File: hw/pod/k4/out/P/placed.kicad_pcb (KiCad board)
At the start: 6 copper layers, 15.5 x 12 mm, 37 parts, among them J1 TestPoint_Pad_D1.0mm, J2 TestPoint_Pad_D1.0mm, J21 CONN-SMD_BM28B0.6-30DP-2-0.35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, Q1 Nexperia_SOT1216_DFN1010B-6, Q2 Nexperia_SOT1216_DFN1010B-6, U1 QFN-48-1EP_7x7mm_P0.5mm_EP5.6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, Y1 Crystal_SMD_2012-2Pin_2.0x1.2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

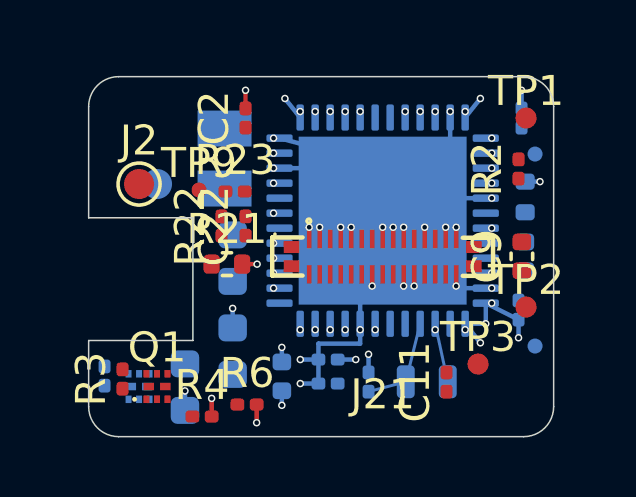
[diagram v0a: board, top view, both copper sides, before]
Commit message: K4 lid ledge 0.70 (ECR-0022) + C21 0402: M re-routed 0/0, heights from datasheets: lid +0.112 floor +0.163 worst, B2B gap side still fails (C16 -0.10, C17/C9 -0.05)
Noise F02->MIC_VDD worst corner 28.7 dB, k4_checks PASS, plm 0/0. P untouched.

Co-Authored-By: Claude Opus 5.5 <noreply@anthropic.com>
Claude-Session: https://claude.ai/code/session_01Wg997D6KFs8bxoAH56jZZJ
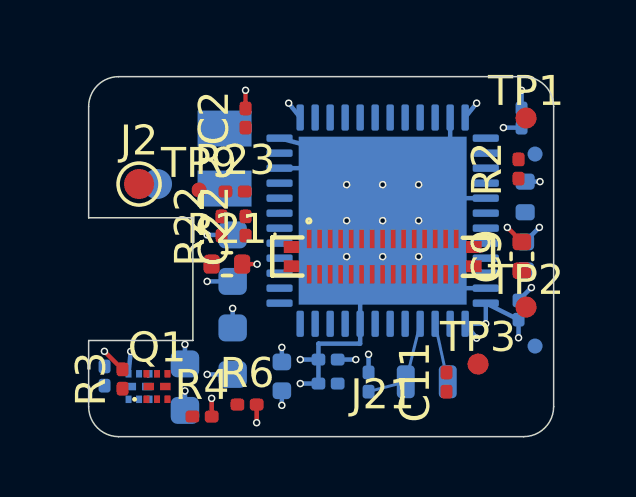
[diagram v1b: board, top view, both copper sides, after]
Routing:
- net GND: track 15.4 -> 18.9 mm, vias 31 -> 25
- net +3V0: track 7.38 -> 10.7 mm, vias 14 -> 13
- net VDD11: vias 2 -> 0
- net VBUS_SENSE: vias 1 -> 0
- net VBAT_SENSE: vias 1 -> 0
- net USB_DP: vias 1 -> 0
- net USB_DM: vias 1 -> 0
- net TS: vias 1 -> 0
- net SWDIO: vias 1 -> 0
- net SWCLK: vias 1 -> 0
- net NRST: vias 1 -> 0
- net N$2: vias 1 -> 0
- net MIC_VDD: vias 1 -> 0
- net MIC_DATA: vias 1 -> 0
- net MDF_SDI: vias 1 -> 0
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
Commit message: K4 guide: BM28 no-key warning, pin-1 dots, photo check, 10-cycle limit
Co-Authored-By: Claude Opus 5.5 <noreply@anthropic.com>
Claude-Session: https://claude.ai/code/session_01Wg997D6KFs8bxoAH56jZZJ
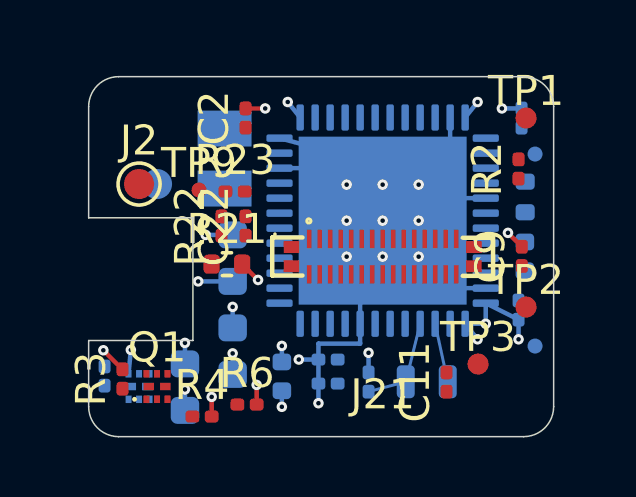
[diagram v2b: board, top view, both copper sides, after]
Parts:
- C9: value C_0402_1005Metric -> C_0201_0603Metric; footprint C_0402_1005Metric -> C_0201_0603Metric
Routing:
- net +3V0: track 10.7 -> 9.78 mm, vias 13 -> 11
- net GND: track 18.9 -> 18.1 mm, vias 25 -> 22
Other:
- copper layers 6 -> 4

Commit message: K4 B2B gap: C16/C17 (M) and C9 (P) to Samsung 0201 (0.39 max): gap side 0 fail, worst +0.05 (U3 BQ25180 / D4 0.5 max are package-fixed); D5 0.45, U3 0.5 from datasheets; M re-routed 0/0, P local edit
Co-Authored-By: Claude Opus 5.5 <noreply@anthropic.com>
Claude-Session: https://claude.ai/code/session_01Wg997D6KFs8bxoAH56jZZJ
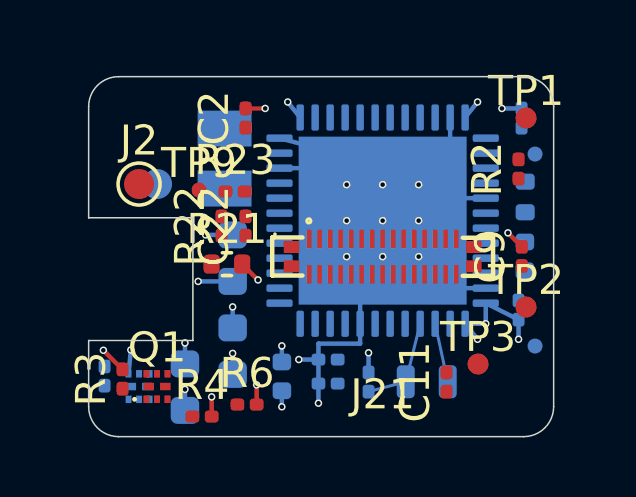
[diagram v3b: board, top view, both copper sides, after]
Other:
- copper layers 4 -> 6
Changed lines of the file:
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@@
 		(4 "In1.Cu" power)
 		(6 "In2.Cu" power)
+		(8 "In3.Cu" signal)
+		(10 "In4.Cu" signal)
 		(2 "B.Cu" signal)
 		(9 "F.Adhes" user "F.Adhesive")
@@
 	(via
 		(at 4.8 9.225)
-		(size 0.35)
+		(size 0.25)
 		(drill 0.15)
 		(layers "F.Cu" "B.Cu")
@@
 	(via
 		(at 6.439999 11.004999)
-		(size 0.35)
+		(size 0.25)
 		(drill 0.15)
 		(layers "F.Cu" "B.Cu")
@@
 	(via
 		(at 6.636139 0.845174)
-		(size 0.35)
+		(size 0.25)
 		(drill 0.15)
 		(layers "F.Cu" "B.Cu")
@@
 	(via
 		(at 14.33 8.754999)
-		(size 0.35)
+		(size 0.25)
 		(drill 0.15)
 		(layers "F.Cu" "B.Cu")
@@
 	(via
 		(at 12.96386 8.754825)
-		(size 0.35)
+		(size 0.25)
 		(drill 0.15)
 		(layers "F.Cu" "B.Cu")
@@
 	(via
 		(at 3.9 5.274999)
-		(size 0.35)
+		(size 0.25)
 		(drill 0.15)
 		(layers "F.Cu" "B.Cu")
@@
 	(via
 		(at 12.96386 0.845174)
-		(size 0.35)
+		(size 0.25)
 		(drill 0.15)
 		(layers "F.Cu" "B.Cu")
@@
 	(via
 		(at 1.407059 9.108719)
-		(size 0.35)
+		(size 0.25)
 		(drill 0.15)
 		(layers "F.Cu" "B.Cu")
@@
 	(via
 		(at 13.2375 8.2375)
-		(size 0.35)
+		(size 0.25)
 		(drill 0.15)
 		(layers "F.Cu" "B.Cu")
@@
 	(via
 		(at 3.21 10.425)
-		(size 0.35)
+		(size 0.25)
 		(drill 0.15)
 		(layers "F.Cu" "B.Cu")
@@
 	(via
 		(at 0.490068 9.120068)
-		(size 0.35)
+		(size 0.25)
 		(drill 0.15)
 		(layers "F.Cu" "B.Cu")
@@
 	(via
 		(at 8.6 3.599999)
-		(size 0.35)
+		(size 0.25)
 		(drill 0.15)
 		(layers "F.Cu" "B.Cu")
@@
 	(via
 		(at 8.6 6)
-		(size 0.35)
+		(size 0.25)
 		(drill 0.15)
 		(layers "F.Cu" "B.Cu")
@@
 	(via
 		(at 5.646794 6.776794)
-		(size 0.35)
+		(size 0.25)
 		(drill 0.15)
 		(layers "F.Cu" "B.Cu")
@@
 	(via
 		(at 7.005 9.43)
-		(size 0.35)
+		(size 0.25)
 		(drill 0.15)
 		(layers "F.Cu" "B.Cu")
@@
 	(via
 		(at 7.66 10.885)
-		(size 0.35)
+		(size 0.25)
 		(drill 0.15)
 		(layers "F.Cu" "B.Cu")
@@
 	(via
 		(at 13.775 1.06)
-		(size 0.35)
+		(size 0.25)
 		(drill 0.15)
 		(layers "F.Cu" "B.Cu")
@@
 	(via
 		(at 5.885 1.06)
-		(size 0.35)
+		(size 0.25)
 		(drill 0.15)
 		(layers "F.Cu" "B.Cu")
@@
 	(via
 		(at 5.6 10.275)
-		(size 0.35)
+		(size 0.25)
 		(drill 0.15)
 		(layers "F.Cu" "B.Cu")
@@
 	(via
 		(at 9.8 6)
-		(size 0.35)
+		(size 0.25)
 		(drill 0.15)
 		(layers "F.Cu" "B.Cu")
@@
 	(via
 		(at 13.976845 5.206845)
-		(size 0.35)
+		(size 0.25)
 		(drill 0.15)
 		(layers "F.Cu" "B.Cu")
@@
 	(via
 		(at 9.33 9.205)
-		(size 0.35)
+		(size 0.25)
 		(drill 0.15)
 		(layers "F.Cu" "B.Cu")
@@
 	(via
 		(at 3.65 6.825)
-		(size 0.35)
+		(size 0.25)
 		(drill 0.15)
 		(layers "F.Cu" "B.Cu")
@@
 	(via
 		(at 11 4.8)
-		(size 0.35)
+		(size 0.25)
 		(drill 0.15)
 		(layers "F.Cu" "B.Cu")
@@
 	(via
 		(at 11 6)
-		(size 0.35)
+		(size 0.25)
 		(drill 0.15)
 		(layers "F.Cu" "B.Cu")
@@
 	(via
 		(at 8.6 4.8)
-		(size 0.35)
+		(size 0.25)
 		(drill 0.15)
 		(layers "F.Cu" "B.Cu")
@@
 	(via
 		(at 3.21 8.875)
-		(size 0.35)
+		(size 0.25)
 		(drill 0.15)
 		(layers "F.Cu" "B.Cu")
@@
 	(via
 		(at 6.439999 8.975)
-		(size 0.35)
+		(size 0.25)
 		(drill 0.15)
 		(layers "F.Cu" "B.Cu")
@@
 	(via
 		(at 9.8 3.599999)
-		(size 0.35)
+		(size 0.25)
 		(drill 0.15)
 		(layers "F.Cu" "B.Cu")
@@
 	(via
 		(at 4.099999 10.675)
-		(size 0.35)
+		(size 0.25)
 		(drill 0.15)
 		(layers "F.Cu" "B.Cu")
@@
 	(via
 		(at 11 3.599999)
-		(size 0.35)
+		(size 0.25)
 		(drill 0.15)
 		(layers "F.Cu" "B.Cu")
@@
 	(via
 		(at 4.8 7.675)
-		(size 0.35)
+		(size 0.25)
 		(drill 0.15)
 		(layers "F.Cu" "B.Cu")
@@
 	(via
 		(at 9.8 4.8)
-		(size 0.35)
+		(size 0.25)
 		(drill 0.15)
 		(layers "F.Cu" "B.Cu")

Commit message: K4 re-place/route after 9ec84ae: P and M at L 15.5, plain kicad-cli DRC 0 errors / 0 unconnected both; route_net3d GRID env; pin-contract + ECR-0020 + backlog (C9/C17 datasheet check still open)
Co-Authored-By: Claude Opus 5.5 <noreply@anthropic.com>
Claude-Session: https://claude.ai/code/session_01Wg997D6KFs8bxoAH56jZZJ
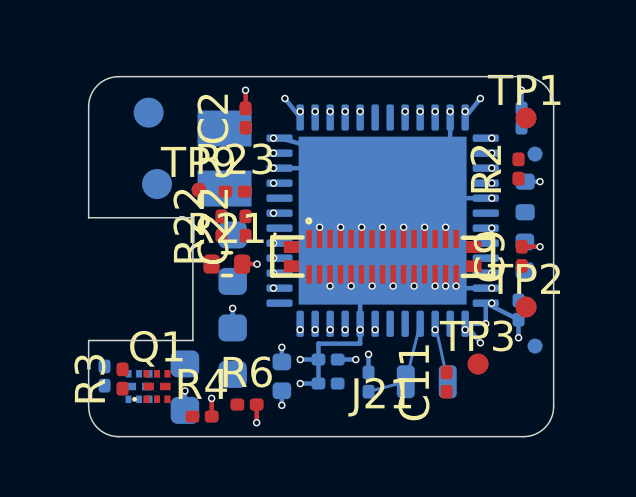
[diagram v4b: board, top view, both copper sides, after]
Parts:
- J2: moved to B.Cu
- moved J2 2.40 mm to (2.00, 1.20), turned to 180 degrees
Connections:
- J21 pad 1: GND -> MIC_VDD
- J21 pad 11: USB_DP -> USB_DM
- J21 pad 13: USB_DM -> USB_DP
- J21 pad 15: GND -> +3V0
- J21 pad 17: +3V0 -> GND
- J21 pad 18: +3V0 -> GND
- J21 pad 19: +3V0 -> LED_K
- J21 pad 21: GND -> MIC_DATA
- J21 pad 22: TS -> GND
- J21 pad 23: I2C_SCL -> CHG_INT
- J21 pad 25: I2C_SDA -> BTN
- J21 pad 26: CHG_INT -> GND
- J21 pad 28: VBAT_SENSE -> GND
- J21 pad 29: BTN -> TS
- J21 pad 30: LED_K -> +3V0
- J21 pad 31: (no net) -> +3V0
- J21 pad 32: (no net) -> +3V0
- J21 pad 33: (no net) -> +3V0
- J21 pad 34: (no net) -> +3V0
- J21 pad 5: GND -> VBAT_SENSE
- J21 pad 6: MIC_VDD -> GND
- J21 pad 7: MIC_DATA -> I2C_SCL
- J21 pad 9: GND -> I2C_SDA
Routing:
- net +3V0: track 9.78 -> 7.38 mm, vias 11 -> 14
- net GND: track 18.1 -> 16.0 mm, vias 22 -> 33
- net VDD11: vias 0 -> 2
- net VBUS_SENSE: vias 0 -> 1
- net VBAT_SENSE: vias 0 -> 1
- net USB_DP: vias 0 -> 1
- net USB_DM: vias 0 -> 1
- net TS: vias 0 -> 1
- net SWDIO: vias 0 -> 1
- net SWCLK: vias 0 -> 1
- net NRST: vias 0 -> 1
- net N$2: vias 0 -> 1
- net MIC_VDD: vias 0 -> 1
- net MIC_DATA: vias 0 -> 1
- net MDF_SDI: vias 0 -> 1
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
